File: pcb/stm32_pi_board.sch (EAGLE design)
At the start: 67 parts, among them IC1 LD1117, IC2 ESP-11, IC3 LD1117, IC4 STM32F405RG, IC5 STF203-22, Q1 BSH205, Q2 N2004, Q5 BSH205, Q6 N2004, X1 PJ-043-SMT, X2 DM3AT, X3 XM7D-0512

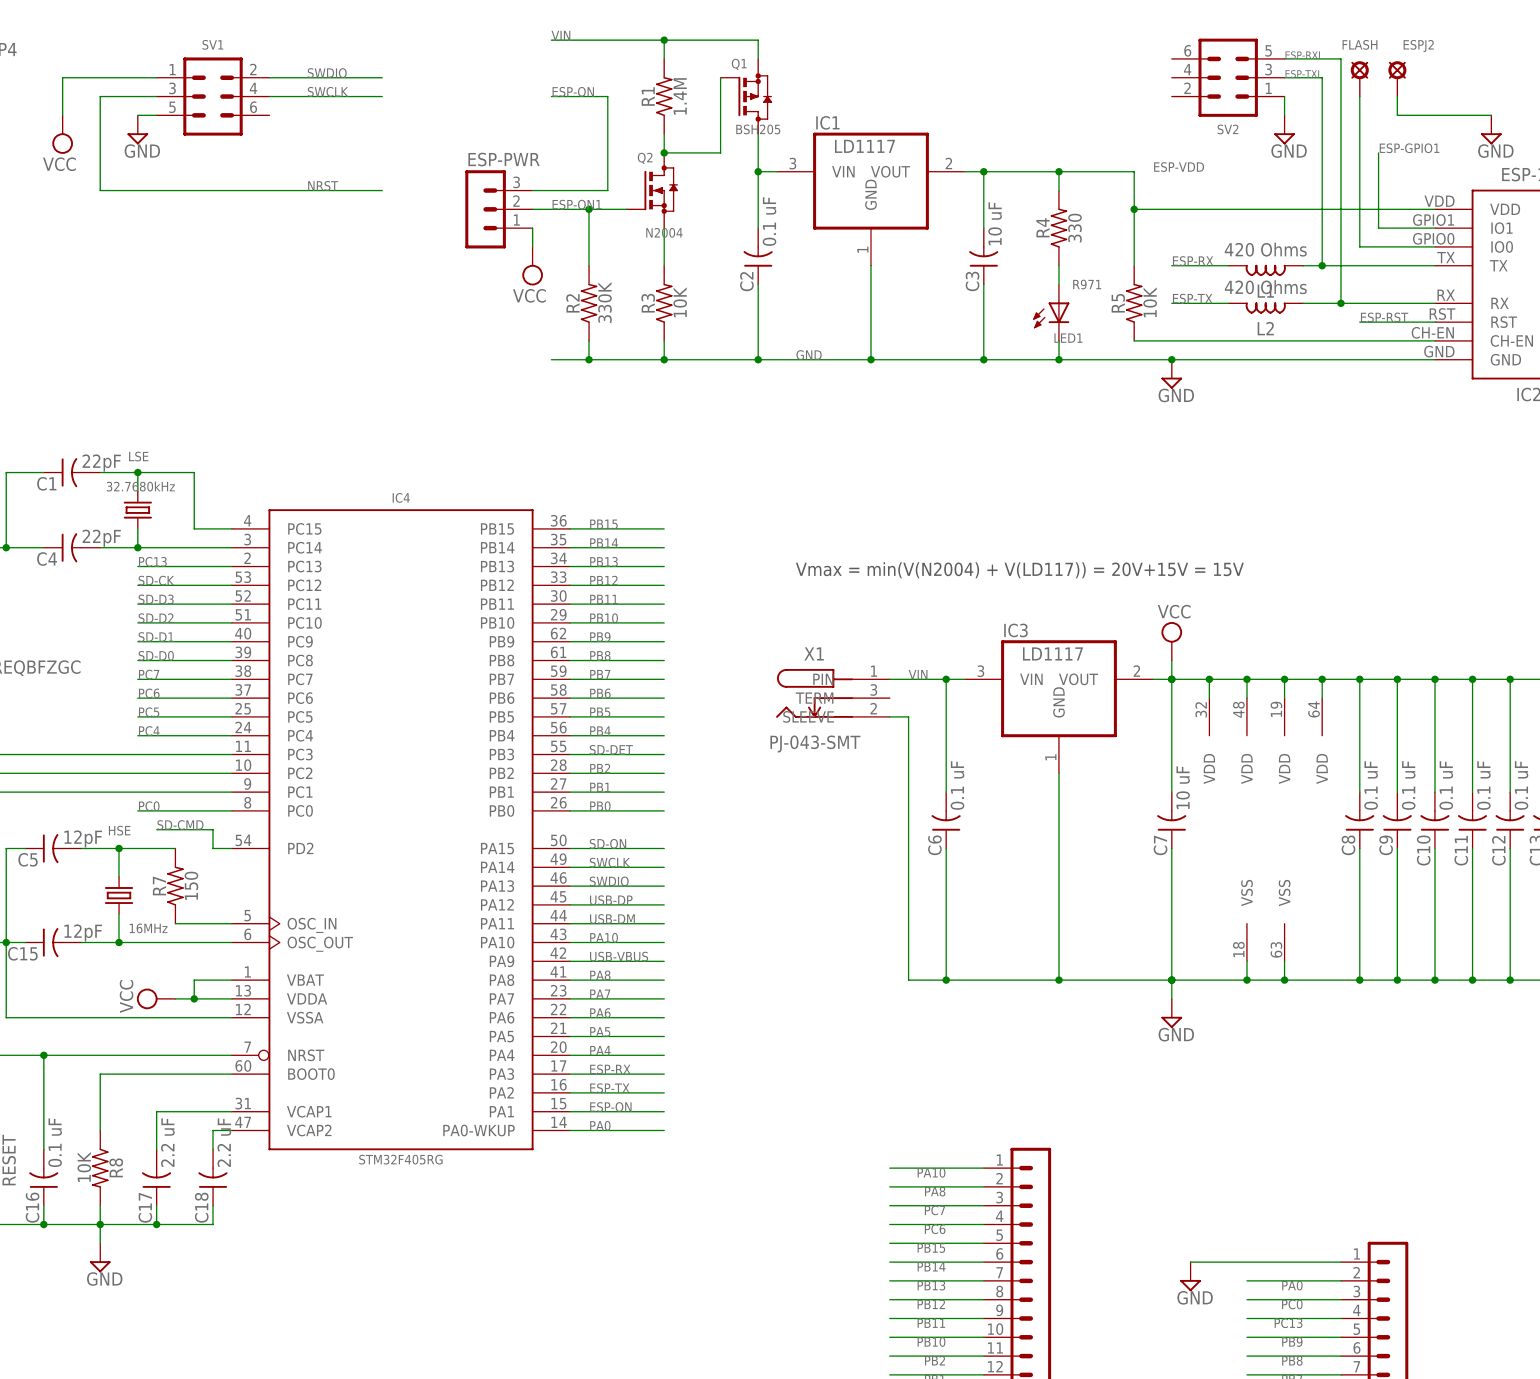
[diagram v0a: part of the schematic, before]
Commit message: Imprved stm32_pi_board
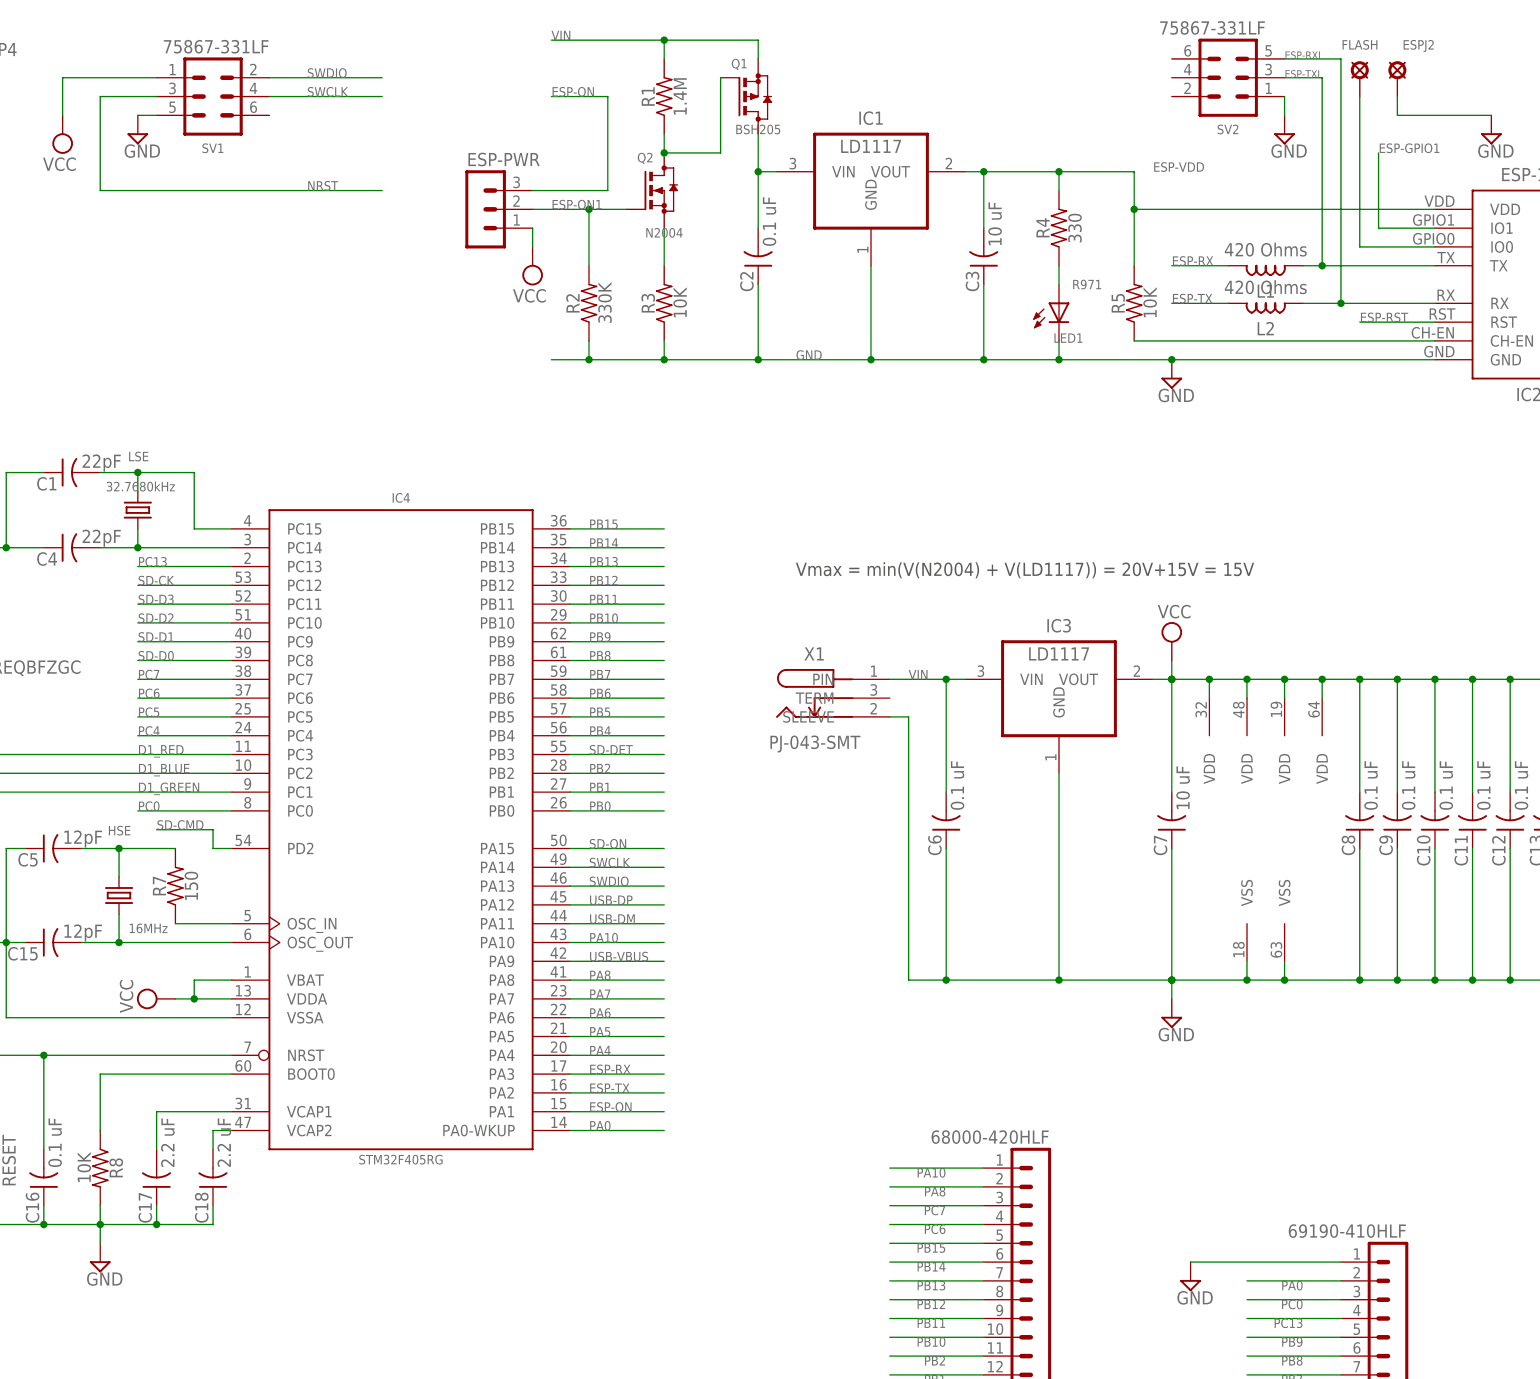
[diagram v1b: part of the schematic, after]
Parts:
- IC1, IC3: device burr-brown:REG1117 -> MyComponents:REG1117
- SV1, SV2: value (none) -> 75867-331LF
- SV4: value (none) -> 68000-420HLF
- SV5: value (none) -> 69190-410HLF
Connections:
- net BOOT1 renamed BOOT
- net N$42 renamed D1_BLUE
- net N$43 renamed D1_RED
- net N$44 renamed D1_GREEN
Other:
- note added: "Vmax = min(V(N2004) + V(LD1117)) = 20V+15V = 15V"
- note removed: "Vmax = min(V(N2004) + V(LD117)) = 20V+15V = 15V"
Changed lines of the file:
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@@
 <part name="SUPPLY37" library="supply2" deviceset="GND" device=""/>
 <part name="X3" library="MyComponents" deviceset="MINI-USB-5-DPI" device="" value="XM7D-0512"/>
-<part name="SV1" library="MyComponents" deviceset="MA03-2" device=""/>
-<part name="SV2" library="MyComponents" deviceset="MA03-2" device=""/>
+<part name="SV1" library="MyComponents" deviceset="MA03-2" device="" value="75867-331LF"/>
+<part name="SV2" library="MyComponents" deviceset="MA03-2" device="" value="75867-331LF"/>
 <part name="X1" library="MyComponents" deviceset="DC-POWER-JACK" device="2" value="PJ-043-SMT"/>
 <part name="IC2" library="MyComponents" deviceset="ESP-11" device=""/>
-<part name="IC3" library="burr-brown" deviceset="REG1117" device="" value="LD1117"/>
+<part name="IC3" library="MyComponents" deviceset="REG1117" device="" value="LD1117"/>
 <part name="C6" library="MyComponents" deviceset="C-US" device="0805" value="0.1 uF"/>
 <part name="C7" library="MyComponents" deviceset="C-US" device="0805" value="10 uF"/>
@@
 <part name="SUPPLY23" library="supply2" deviceset="GND" device=""/>
 <part name="C12" library="MyComponents" deviceset="C-US" device="0805" value="0.1 uF"/>
-<part name="SV4" library="MyComponents" deviceset="MA20-1" device="NO-PL"/>
-<part name="SV5" library="MyComponents" deviceset="MA10-1" device="NO-PL"/>
+<part name="SV4" library="MyComponents" deviceset="MA20-1" device="NO-PL" value="68000-420HLF"/>
+<part name="SV5" library="MyComponents" deviceset="MA10-1" device="NO-PL" value="69190-410HLF"/>
 <part name="D1" library="MyComponents" deviceset="RGB-LED-5MM" device="" value="WP154A4SUREQBFZGC"/>
 <part name="R6" library="MyComponents" deviceset="R-US" device="0805" value="330"/>
@@
 <part name="R2" library="MyComponents" deviceset="R-US" device="0805" value="330K"/>
 <part name="Q1" library="MyComponents" deviceset="BSH205G2R" device="" value="BSH205"/>
-<part name="IC1" library="burr-brown" deviceset="REG1117" device="" value="LD1117"/>
+<part name="IC1" library="MyComponents" deviceset="REG1117" device="" value="LD1117"/>
 <part name="C2" library="MyComponents" deviceset="C-US" device="0805" value="0.1 uF"/>
 <part name="C3" library="MyComponents" deviceset="C-US" device="0805" value="10 uF"/>
@@
 <description>Centrale and sensor</description>
 <plain>
-<text x="165.1" y="181.61" size="1.778" layer="97">Vmax = min(V(N2004) + V(LD117)) = 20V+15V = 15V</text>
+<text x="165.1" y="181.61" size="1.778" layer="97">Vmax = min(V(N2004) + V(LD1117)) = 20V+15V = 15V</text>
 </plain>
 <instances>
@@
 <instance part="X3" gate="G41" x="259.08" y="15.24"/>
 <instance part="SV1" gate="1" x="86.36" y="246.38" smashed="yes" rot="R180">
-<attribute name="VALUE" x="90.17" y="254" size="1.778" layer="96" rot="R180"/>
-<attribute name="NAME" x="86.36" y="254" size="1.27" layer="95" rot="R180" align="bottom-center"/>
+<attribute name="VALUE" x="93.98" y="254" size="1.778" layer="96" rot="R180"/>
+<attribute name="NAME" x="86.36" y="238.76" size="1.27" layer="95" align="bottom-center"/>
 </instance>
 <instance part="SV2" gate="1" x="223.52" y="248.92" smashed="yes">
-<attribute name="VALUE" x="219.71" y="241.3" size="1.778" layer="96"/>
+<attribute name="VALUE" x="228.6" y="256.54" size="1.778" layer="96" rot="R180"/>
 <attribute name="NAME" x="223.52" y="241.3" size="1.27" layer="95" align="bottom-center"/>
 </instance>
@@
 </segment>
 </net>
-<net name="BOOT1" class="0">
+<net name="BOOT" class="0">
 <segment>
 <pinref part="R8" gate="G$1" pin="1"/>
@@
 </segment>
 </net>
-<net name="N$42" class="0">
+<net name="D1_BLUE" class="0">
 <segment>
 <pinref part="D1" gate="1" pin="AB"/>
 <pinref part="IC4" gate="MCU" pin="PC2"/>
 <wire x1="50.8" y1="154.94" x2="88.9" y2="154.94" width="0.1524" layer="91"/>
-</segment>
-</net>
-<net name="N$43" class="0">
+<label x="76.2" y="154.94" size="1.27" layer="95"/>
+</segment>
+</net>
+<net name="D1_RED" class="0">
 <segment>
 <pinref part="D1" gate="1" pin="AR"/>
@@
 <pinref part="IC4" gate="MCU" pin="PC3"/>
 <wire x1="53.34" y1="157.48" x2="88.9" y2="157.48" width="0.1524" layer="91"/>
-</segment>
-</net>
-<net name="N$44" class="0">
+<label x="76.2" y="157.48" size="1.27" layer="95"/>
+</segment>
+</net>
+<net name="D1_GREEN" class="0">
 <segment>
 <pinref part="IC4" gate="MCU" pin="PC1"/>
@@
 <pinref part="D1" gate="1" pin="AG"/>
 <wire x1="53.34" y1="147.32" x2="50.8" y2="147.32" width="0.1524" layer="91"/>
-</segment>
-</net>
+<label x="76.2" y="152.4" size="1.27" layer="95"/>
+</segment>
+</net>
